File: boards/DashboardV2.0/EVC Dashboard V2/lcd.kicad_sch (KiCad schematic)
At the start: 0 parts

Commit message: Added LCD 40 pos connector symbol
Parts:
- added J2: 62684-402100ALF, 62684-402100ALF:AMPHENOL_62684-402100ALF, symbol LEDs & Displays:62684-402100ALF
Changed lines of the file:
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@@
 	(generator_version "10.0")
 	(paper "A4")
+	(symbol
+		(lib_id "LEDs & Displays:62684-402100ALF")
+		(at 160.02 95.25 0)
+		(unit 1)
+		(body_style 1)
+		(exclude_from_sim no)
+		(in_bom yes)
+		(on_board yes)
+		(in_pos_files yes)
+		(dnp no)
+		(fields_autoplaced yes)
+		(property "Reference" "J2"
+			(at 168.91 93.9799 0)
+			(show_name no)
+			(do_not_autoplace no)
+			(effects
+				(font
+					(size 1.27 1.27)
+				)
+				(justify left)
+			)
+		)
+		(property "Value" "62684-402100ALF"
+			(at 168.91 96.5199 0)
+			(show_name no)
+			(do_not_autoplace no)
+			(effects
+				(font
+					(size 1.27 1.27)
+				)
+				(justify left)
+			)
+		)
+		(property "Footprint" "62684-402100ALF:AMPHENOL_62684-402100ALF"
+			(at 160.02 95.25 0)
+			(hide yes)
+			(show_name no)
+			(do_not_autoplace no)
+			(effects
+				(font
+					(size 1.27 1.27)
+				)
+				(justify bottom)
+			)
+		)
+		(property "Datasheet" ""
+			(at 160.02 95.25 0)
+			(hide yes)
+			(show_name no)
+			(do_not_autoplace no)
+			(effects
+				(font
+					(size 1.27 1.27)
+				)
+			)
+		)
+		(property "Description" "CONN FPC TOP 40POS 0.5MM R/A for display 40pos ribbon cable"
+			(at 160.02 95.25 0)
+			(hide yes)
+			(show_name no)
+			(do_not_autoplace no)
+			(effects
+				(font
+					(size 1.27 1.27)
+				)
+			)
+		)
+		(property "PARTREV" "AK"
+			(at 160.02 95.25 0)
+			(hide yes)
+			(show_name no)
+			(do_not_autoplace no)
+			(effects
+				(font
+					(size 1.27 1.27)
+				)
+				(justify bottom)
+			)
+		)
+		(property "STANDARD" "Manufacturer Recommendations"
+			(at 160.02 95.25 0)
+			(hide yes)
+			(show_name no)
+			(do_not_autoplace no)
+			(effects
+				(font
+					(size 1.27 1.27)
+				)
+				(justify bottom)
+			)
+		)
+		(property "MAXIMUM_PACKAGE_HEIGHT" "2.00mm"
+			(at 160.02 95.25 0)
+			(hide yes)
+			(show_name no)
+			(do_not_autoplace no)
+			(effects
+				(font
+					(size 1.27 1.27)
+				)
+				(justify bottom)
+			)
+		)
+		(property "MANUFACTURER" "Amphenol"
+			(at 160.02 95.25 0)
+			(hide yes)
+			(show_name no)
+			(do_not_autoplace no)
+			(effects
+				(font
+					(size 1.27 1.27)
+				)
+				(justify bottom)
+			)
+		)
+		(pin "15"
+		)
+		(pin "19"
+		)
+		(pin "17"
+		)
+		(pin "20"
+		)
+		(pin "18"
+		)
+		(pin "14"
+		)
+		(pin "16"
+		)
+		(pin "26"
+		)
+		(pin "24"
+		)
+		(pin "23"
+		)
+		(pin "31"
+		)
+		(pin "27"
+		)
+		(pin "28"
+		)
+		(pin "29"
+		)
+		(pin "25"
+		)
+		(pin "21"
+		)
+		(pin "30"
+		)
+		(pin "22"
+		)
+		(pin "35"
+		)
+		(pin "32"
+		)
+		(pin "38"
+		)
+		(pin "34"
+		)
+		(pin "37"
+		)
+		(pin "36"
+		)
+		(pin "40"
+		)
+		(pin "S2"
+		)
+		(pin "33"
+		)
+		(pin "39"
+		)
+		(pin "S1"
+		)
+		(pin "01"
+		)
+		(pin "07"
+		)
+		(pin "06"
+		)
+		(pin "02"
+		)
+		(pin "08"
+		)
+		(pin "03"
+		)
+		(pin "05"
+		)
+		(pin "04"
+		)
+		(pin "12"
+		)
+		(pin "10"
+		)
+		(pin "13"
+		)
+		(pin "11"
+		)
+		(pin "09"
+		)
+		(instances
+			(project "EVC Dashboard V2"
+				(path "/ede78d5d-1d5c-4e8d-a13e-c039265851a9/3ee3826b-6fc5-49c7-b040-60fa39243ad2"
+					(reference "J2")
+					(unit 1)
+				)
+			)
+		)
+	)
 )

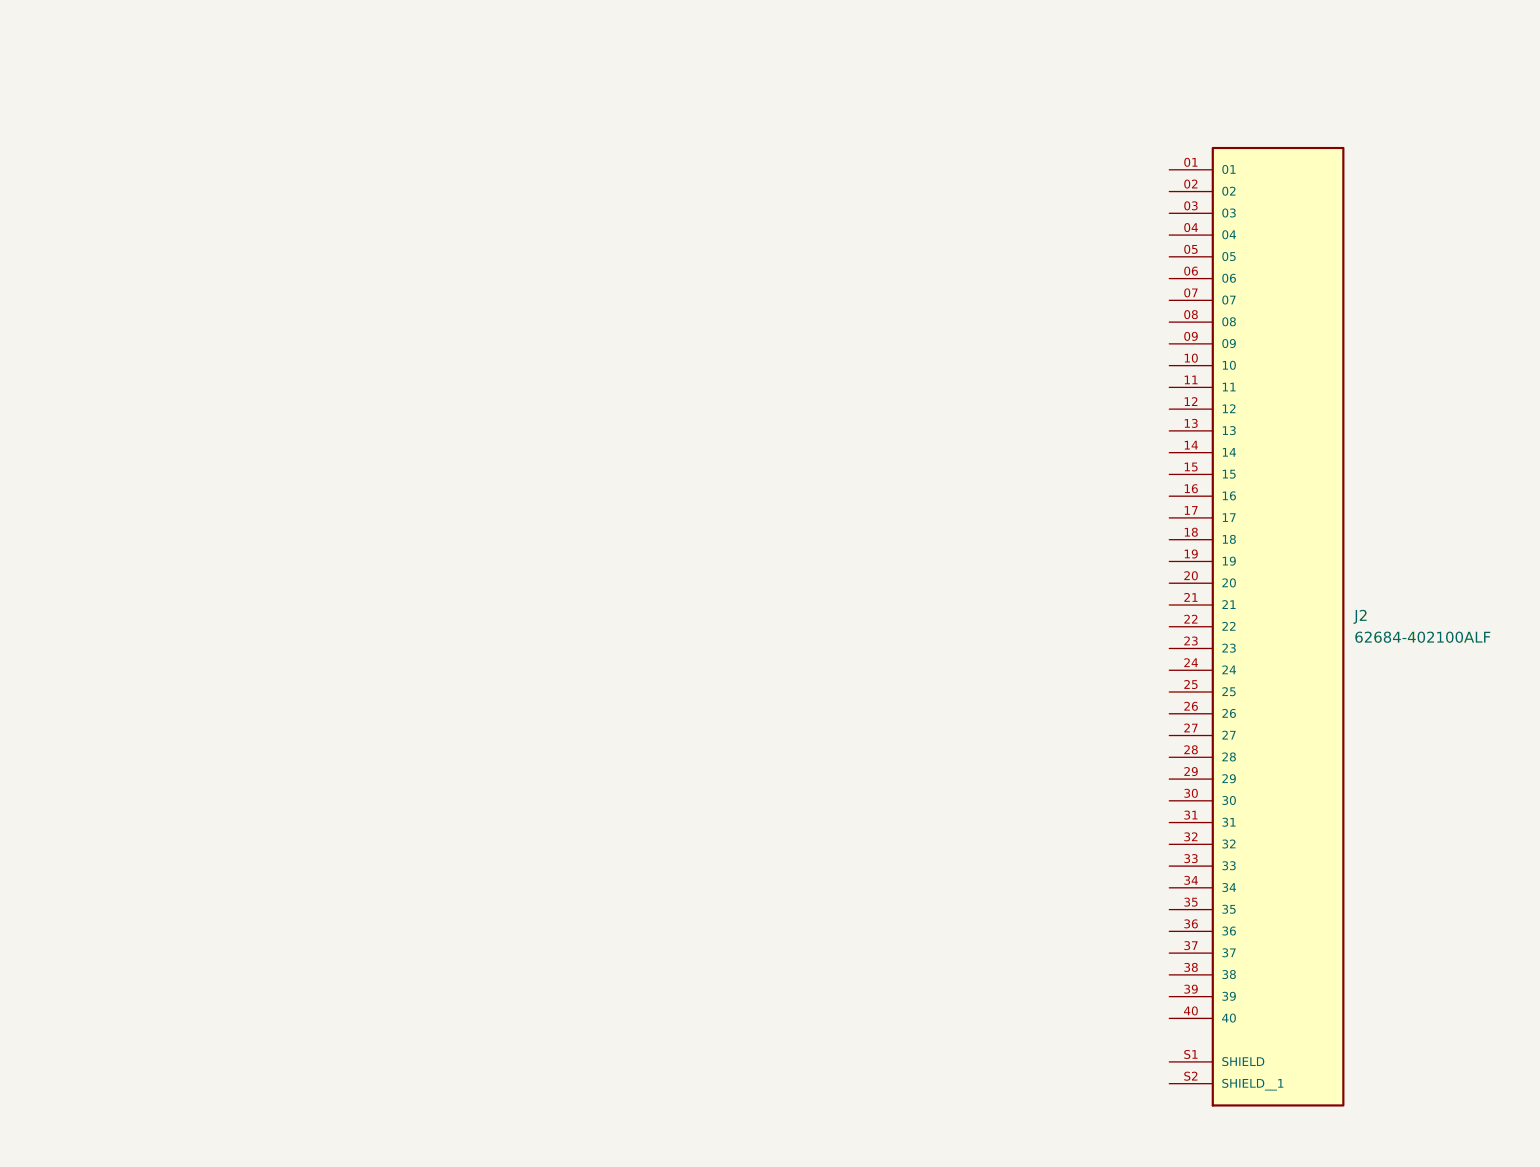
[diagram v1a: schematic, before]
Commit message: Added DCX global label and added connections for 40pos display
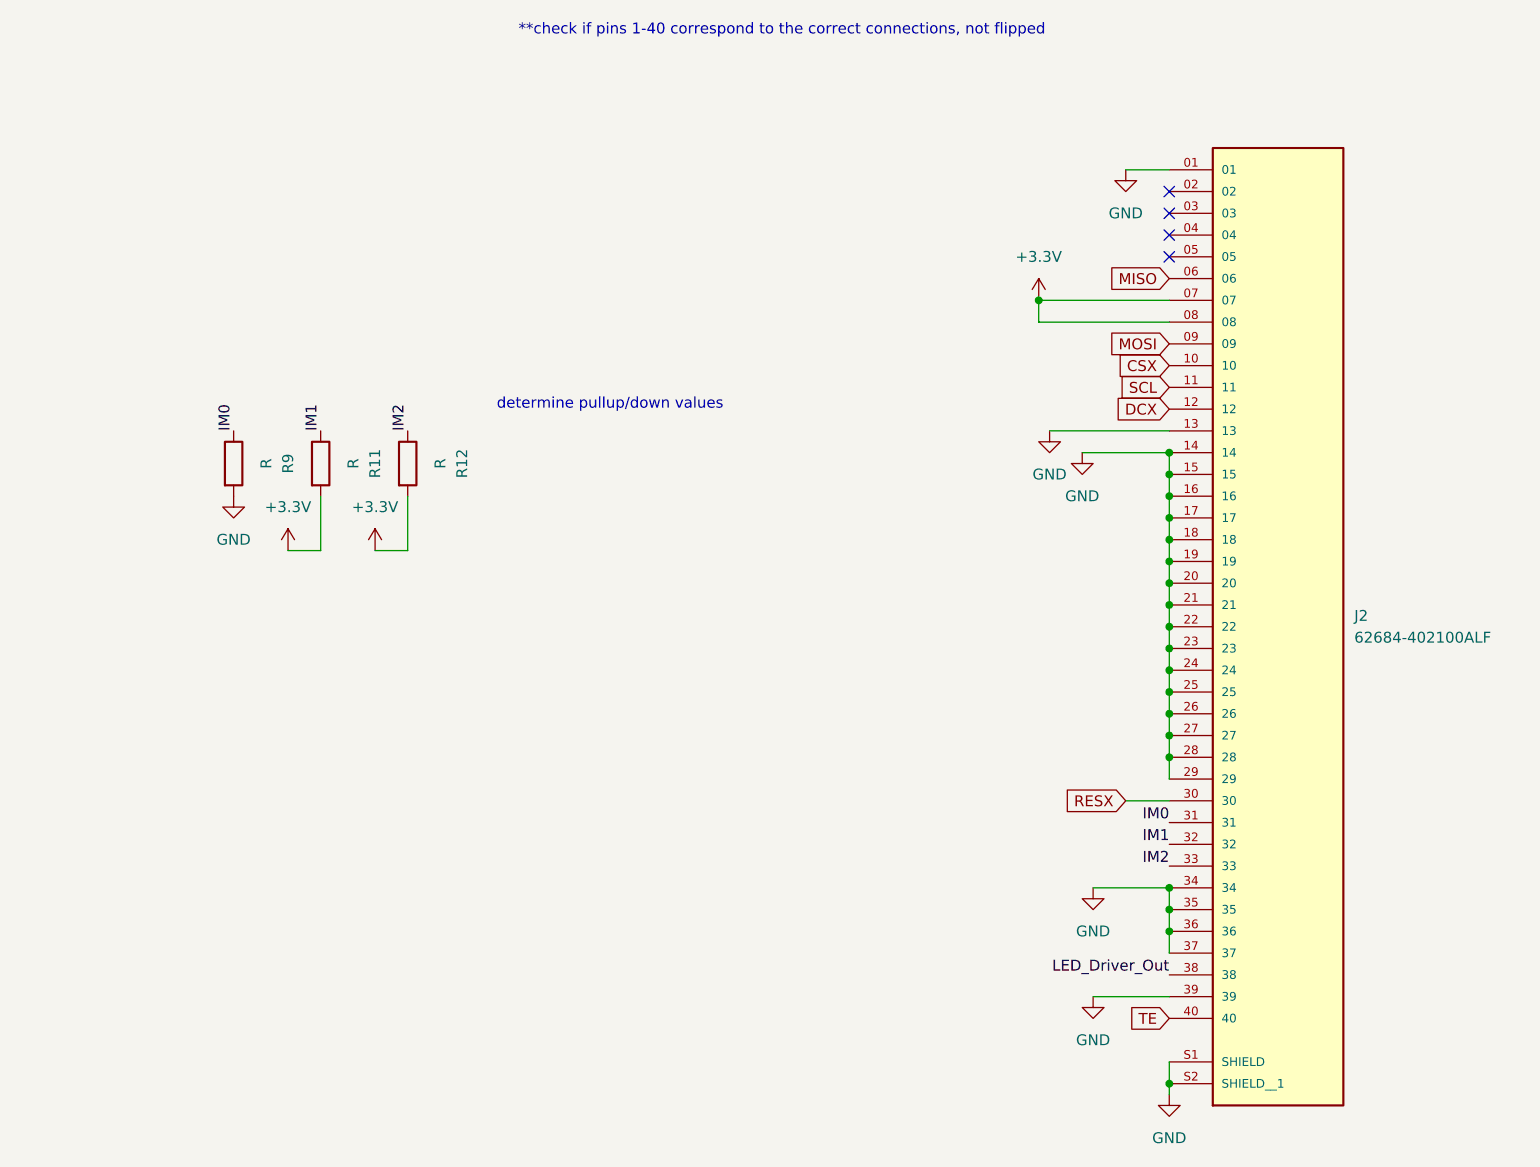
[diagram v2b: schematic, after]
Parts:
- added R11, R12, R9: R, symbol Device:R
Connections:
- net GND: now reaches J2.01
- net GND: now also J2.13, J2.14, J2.15, J2.16, J2.17, J2.18, J2.19, J2.20, J2.21, J2.22, J2.23, J2.24, J2.25, J2.26, J2.27, J2.28, J2.29, J2.34, J2.35, J2.36, J2.37, J2.39, J2.S1 (SHIELD), J2.S2 (SHIELD__1), R9.2
- net MISO: now reaches J2.06
- net +3.3V: now reaches J2.07
- net +3.3V: now also J2.08, R11.2, R12.2
- net MOSI: now reaches J2.09
- net CSX: now reaches J2.10
- net SCL: now reaches J2.11
- net DCX: now reaches J2.12
- net RESX: now reaches J2.30
- net IM0: now reaches J2.31
- net IM0: now also R9.1
- net IM1: now reaches J2.32
- net IM1: now also R11.1
- net IM2: now reaches J2.33
- net IM2: now also R12.1
- net LED_Driver_Out: now reaches J2.38
- net TE: now reaches J2.40
- no-connect marks 0 -> 4
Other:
- note added: "**check if pins 1-40 correspond to the correct connections, not flipped"
- note added: "determine pullup/down values"

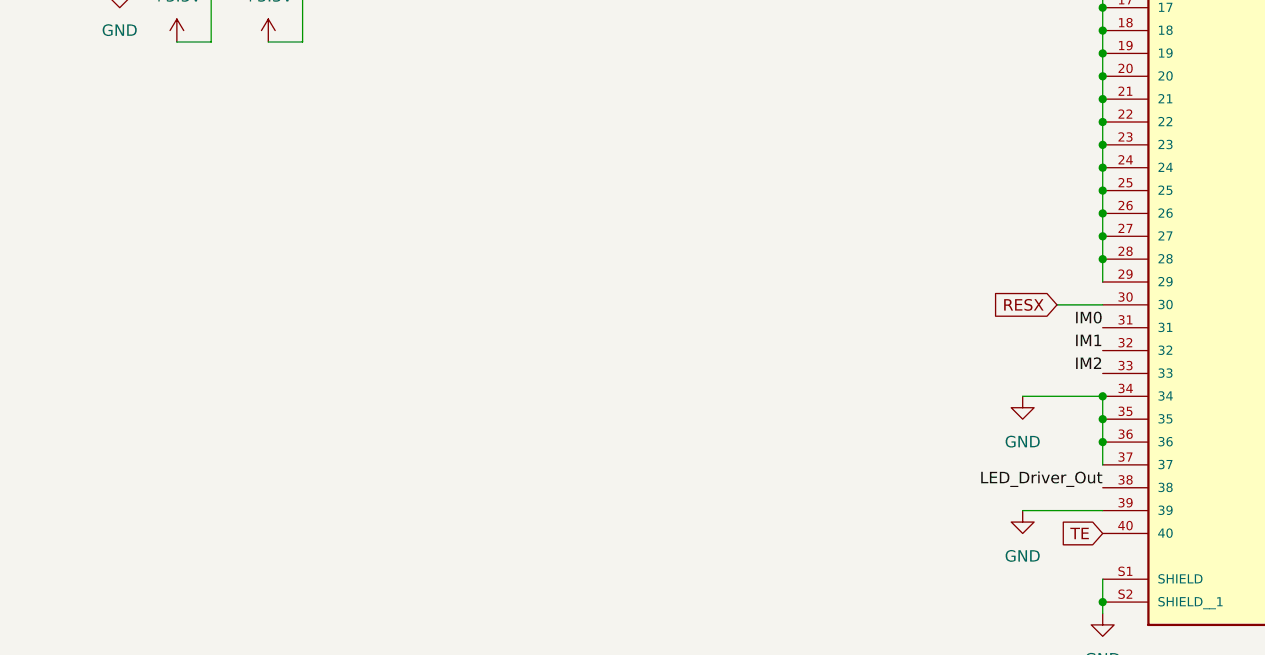
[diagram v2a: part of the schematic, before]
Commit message: Added Backlight Driver
Added the driver schematic and some connections, will finish adding connections
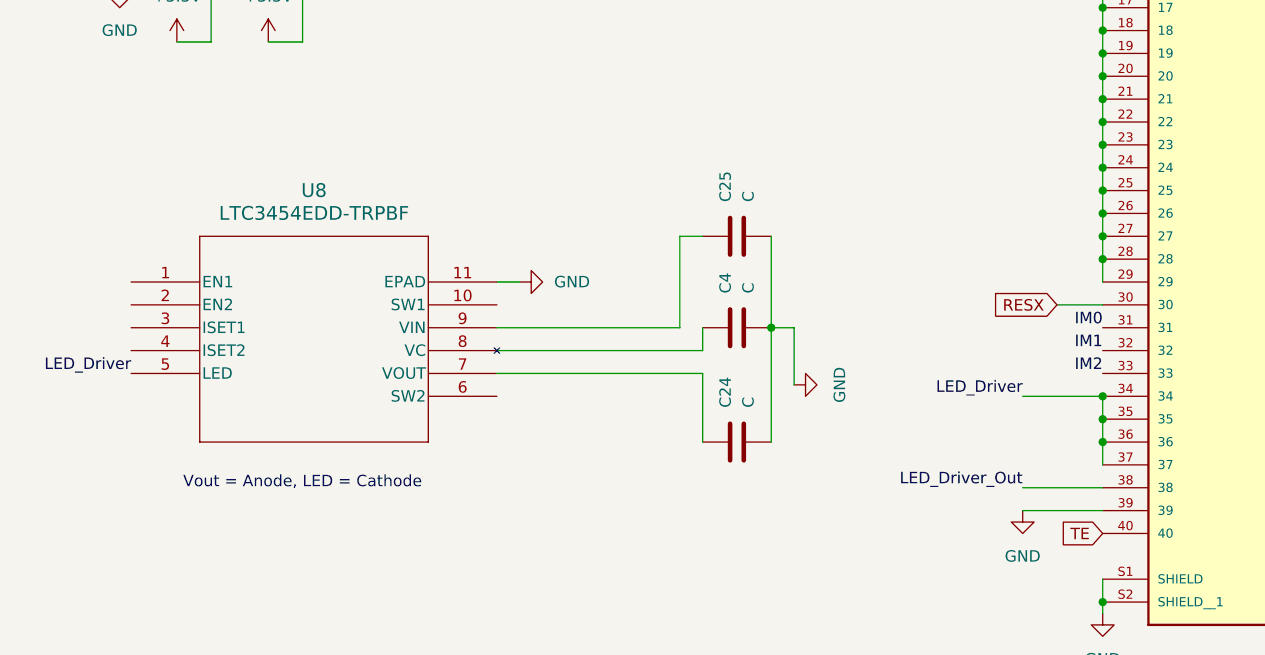
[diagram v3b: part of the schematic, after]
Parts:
- added C24, C25: C, symbol Device:C
- added C4: C, Package_SO:SOIC-8_3.9x4.9mm_P1.27mm, symbol Device:C
- added U8: LTC3454EDD-TRPBF, DFN-10_DD_LIT, symbol Backlight Driver:LTC3454EDD-TRPBF
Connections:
- net GND: now also C24.2, C25.2, C4.2, U8.11 (EPAD); no longer J2.34, J2.35, J2.36, J2.37
- new net: C4.1, U8.8 (VC)
- new net: C24.1, U8.7 (VOUT)
- new net: C25.1, U8.9 (VIN)
- new net LED_Driver: J2.34, J2.35, J2.36, J2.37, U8.5 (LED)
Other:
- note added: "Vout = Anode, LED = Cathode"

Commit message: Finished backlight driver
Finished backlight driver connections and display connections, will add connector to finish
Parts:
- added L1: 4.7uH, symbol Device:L
- added R14: 20.5k, Package_SO:SOIC-8_3.9x4.9mm_P1.27mm, symbol Device:R
- C24, C25: value C -> 10uF
- C4: value C -> 0.1uF
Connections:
- net IM0 is gone; now on net GND: J2.31, R9.1
- net IM1 is gone; now on net GND: J2.32, R11.1
- net IM2 is gone; now on net +3.3V: J2.33, R12.1
- net +3.3V: now also U8.1 (EN1)
- net GND: now also U8.2 (EN2), R14.2
- net at U8.10 (SW1): now also L1.1
- net at U8.3 (ISET1): now also R14.1
- net at U8.6 (SW2): now also L1.2
- no-connect marks 4 -> 5
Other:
- note added: "Only using the 4 wire SPI version"
